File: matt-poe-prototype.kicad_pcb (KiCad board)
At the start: 2 copper layers, 123 x 91.6 mm, 57 parts, among them J2 Conn_02x02_Odd_Even, T1 EP475SG-10, U2 MP8017GL-Z, U4 AP62250WU-7

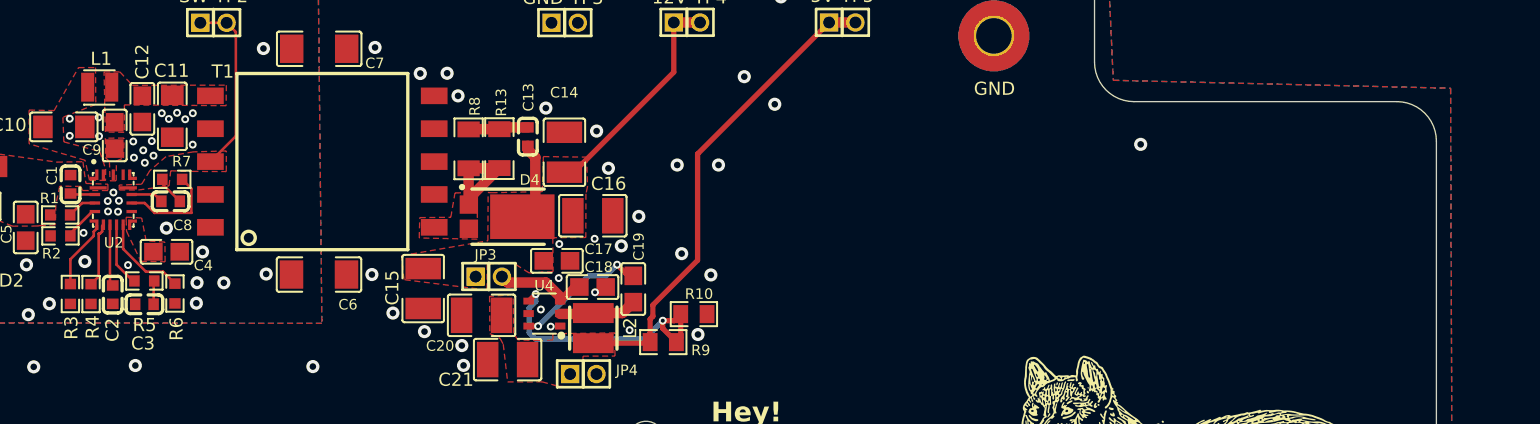
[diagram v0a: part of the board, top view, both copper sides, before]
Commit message: Some component substitutions for optimization and for part availability.
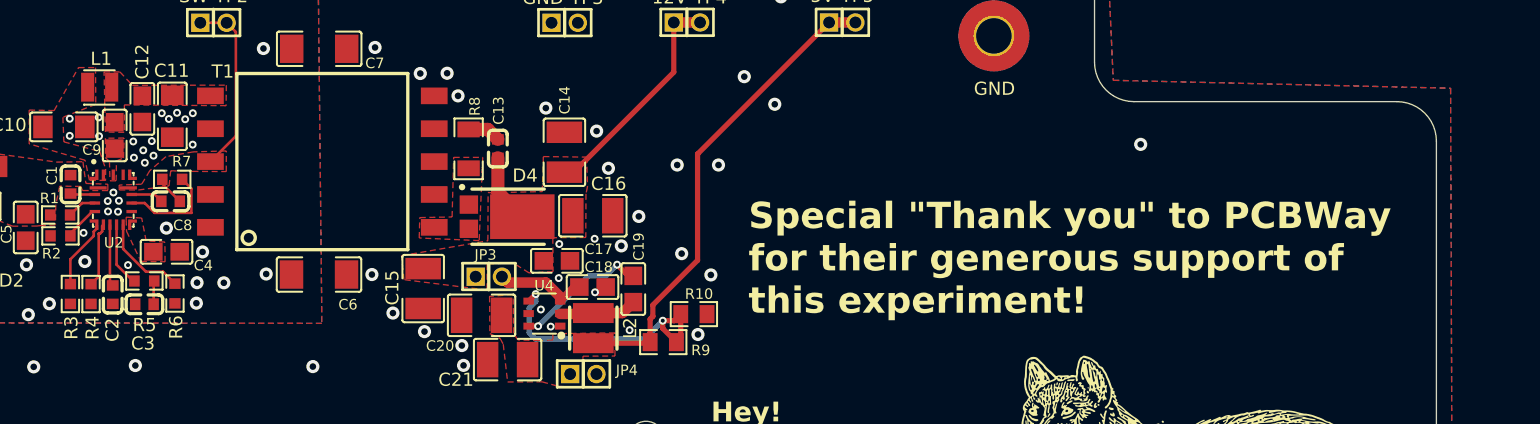
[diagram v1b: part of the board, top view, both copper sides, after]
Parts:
- removed R13: 20Ω, JLCImport:R_1206_C17903
- C13: value 470pF 100V -> 220pF 100V; footprint JLCImport:C_0603_C107062 -> JLCImport:GCM1885C2A221JA16D
- D4: value SBRT20M60SP5-13 -> SBRT20U60SP5-7; footprint JLCImport:D_POWERDI5_C5245040 -> JLCImport:SBRT20U60SP5-7
- R4: value 7.5kΩ -> 9.1kΩ; footprint JLCImport:R_0603_C23234 -> JLCImport:FRC0603J912_TS
- R6: value 150kΩ -> 330kΩ; footprint JLCImport:R_0603_C22807 -> JLCImport:0603WAF3303T5E
- U2: value MP8017GL-Z -> TPE15017
- moved C13 2.45 mm to (178.4, 31.4)
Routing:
- net Net-(D4-Pad1): track 8.83 -> 0.03 mm
- net Net-(C13-Pad1): track 4.57 -> 2.54 mm
- net +12V: track 23.3 -> 22.5 mm
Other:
- board text added: "Special {dblquote}Thank you{dblquote} to PCBWay for their generous support of this experiment!"
